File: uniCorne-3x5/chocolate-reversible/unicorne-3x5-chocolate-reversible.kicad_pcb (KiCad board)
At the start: 2 copper layers, 114.7 x 91.4 mm, 87 parts, among them J1 MJ-4PP-9, J2 Conn_01x05, J3 Conn_01x02, J4 Conn_01x03, SW1 SW_CHOC_HS, SW10 SW_CHOC_HS, SW11 SW_CHOC_HS, SW12 SW_CHOC_HS, SW13 SW_CHOC_HS, SW14 SW_CHOC_HS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

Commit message: amended chocolate 3x5
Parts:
- U1: footprint TB2086_MISC:ProMicro-ish-dn-rev-unrouted_3x5 -> TB2086_MISC:ProMicro-ish-dn-rev-unrouted_3x6
- moved R3 1.75 mm to (183.5, 110.0)
- moved R4 1.75 mm to (183.5, 111.9)
- moved JP9 1.22 mm to (187.7, 111.0)
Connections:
- PSW1 pad 1: unconnected-(PSW1-A-Pad1) -> BAT+
- PSW1 pad 3: BAT+ -> unconnected-(PSW1-C-Pad3)
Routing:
- net unconnected-(U1-RAW-Pad24): track 29.2 -> 11.0 mm
- net DATA: track 64.2 -> 75.9 mm
- net unconnected-(PSW1-C-Pad3): track 0.00 -> 6.49 mm
- net unconnected-(PSW1-A-Pad1): track 6.23 -> 0.00 mm
- net LED: track 61.5 -> 65.6 mm, vias 4 -> 5
- net BAT+: track 17.4 -> 14.1 mm
- net col2: track 192.9 -> 195.2 mm
- net unconnected-(U1-B3-Pad15): track 18.6 -> 16.5 mm
- net SDA: track 72.7 -> 70.8 mm
- net SCL: track 59.4 -> 61.2 mm
- net GND: track 45.4 -> 46.7 mm, vias 23 -> 24
- net Net-(JP9-C): track 16.3 -> 15.4 mm
- net col0: track 206.5 -> 205.6 mm
- net col1: track 187.2 -> 186.5 mm
- net row0: track 147.8 -> 148.2 mm, vias 1 -> 2
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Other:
- board text added: "uniCorne Choc 3x5"
- board text removed: "uniCorne Choc"

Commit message: small tweak
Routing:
- net RESET: track 59.3 -> 61.7 mm
- net IS_LEFT: track 24.6 -> 22.3 mm
- net unconnected-(PSW1-C-Pad3): track 6.49 -> 5.34 mm
- net Net-(JP9-C): track 15.4 -> 14.4 mm
- net SCL: track 61.2 -> 60.3 mm
- net SDA: track 70.8 -> 70.1 mm
- net col4: track 136.5 -> 135.9 mm
- net DATA: track 75.9 -> 75.3 mm
- net GND: track 46.7 -> 46.3 mm, vias 24 -> 23

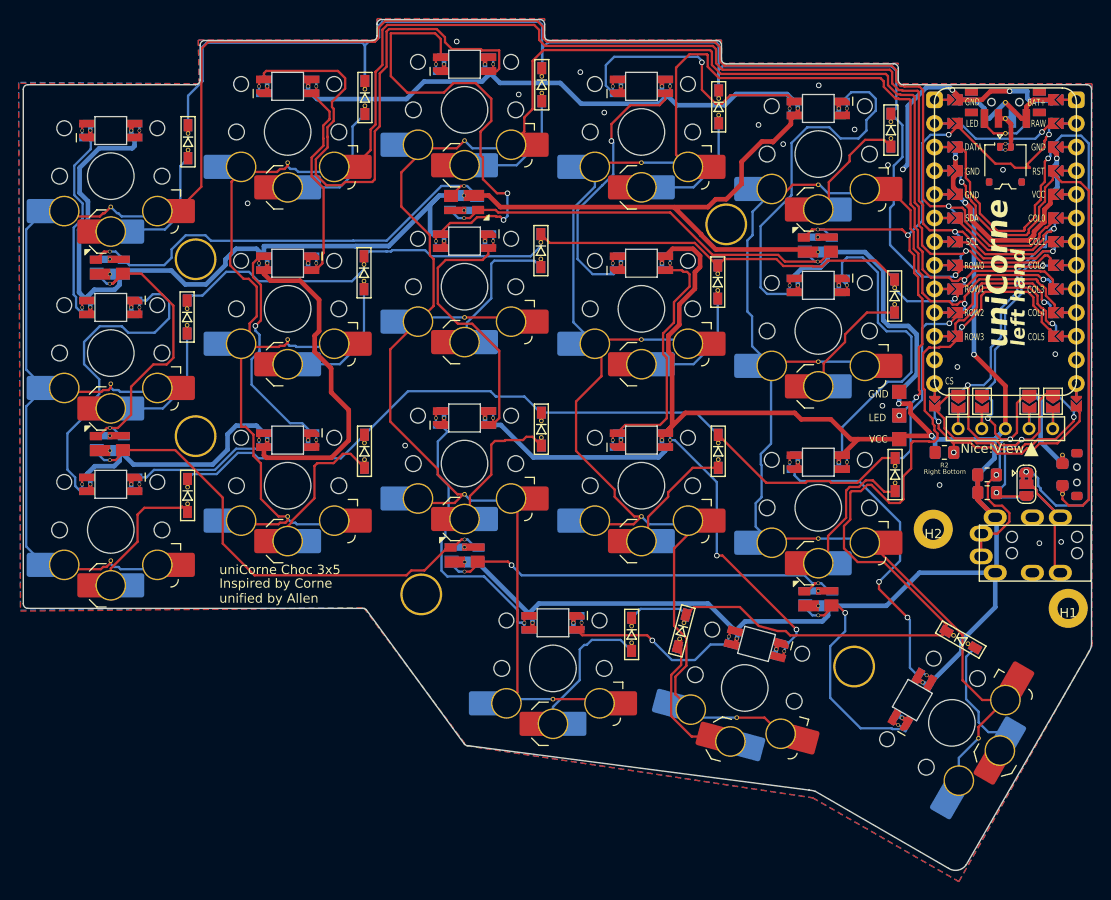
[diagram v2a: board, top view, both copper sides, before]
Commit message: amended footprint for LED
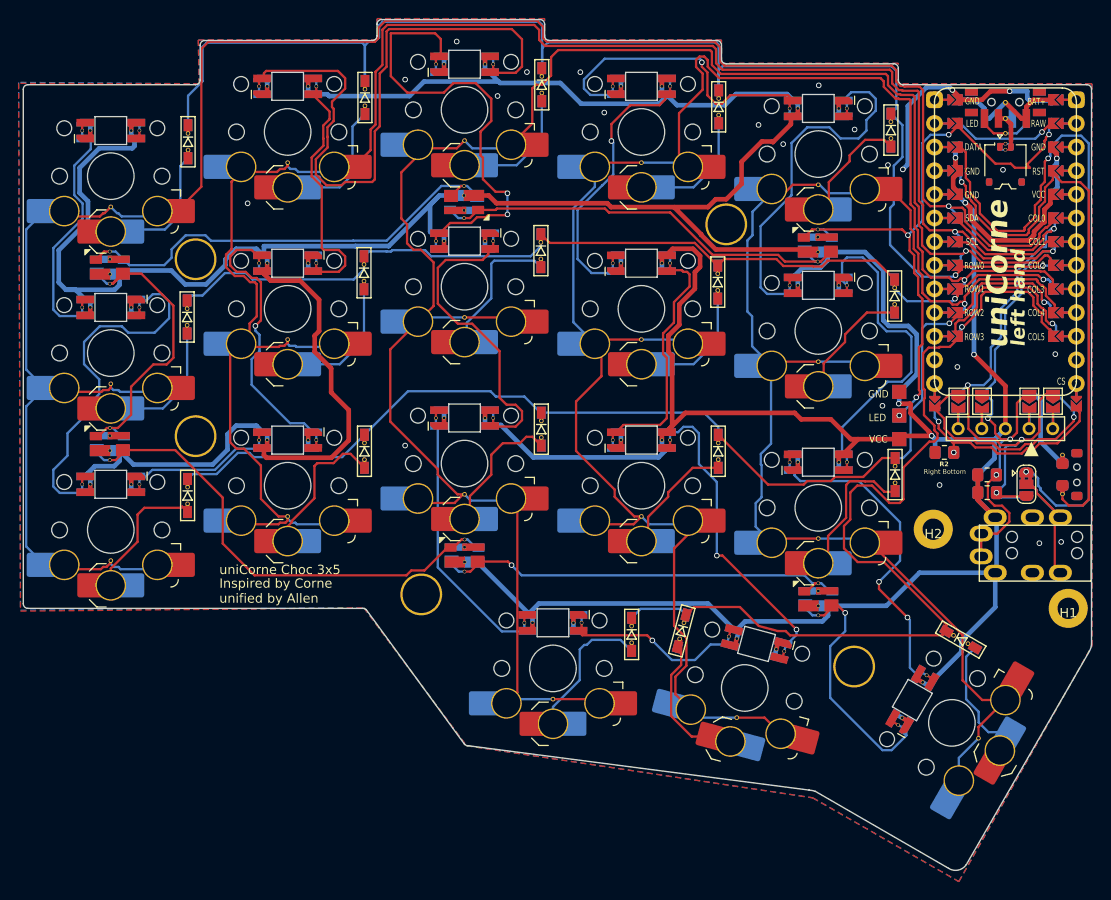
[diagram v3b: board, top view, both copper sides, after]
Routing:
- net Net-(L12-DIN): track 23.6 -> 29.0 mm
- net Net-(L2-DIN): track 61.9 -> 66.9 mm
- net Net-(L13-DOUT): track 27.5 -> 31.9 mm
- net Net-(L2-DOUT): track 21.5 -> 25.8 mm
- net Net-(L4-DIN): track 28.6 -> 32.3 mm
- net Net-(L1-DIN): track 21.1 -> 24.4 mm
- net Net-(L14-DOUT): track 28.5 -> 31.6 mm
- net Net-(L11-DOUT): track 35.6 -> 38.2 mm
- net Net-(L18-DIN): track 25.2 -> 27.7 mm
- net VCC: track 518.8 -> 521.2 mm
- net col1: track 186.0 -> 188.0 mm
- net Net-(L13-DIN): track 29.3 -> 27.5 mm
- net col3: track 178.0 -> 176.7 mm
- net row3: track 109.4 -> 108.3 mm
- net CS: track 25.9 -> 25.0 mm
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
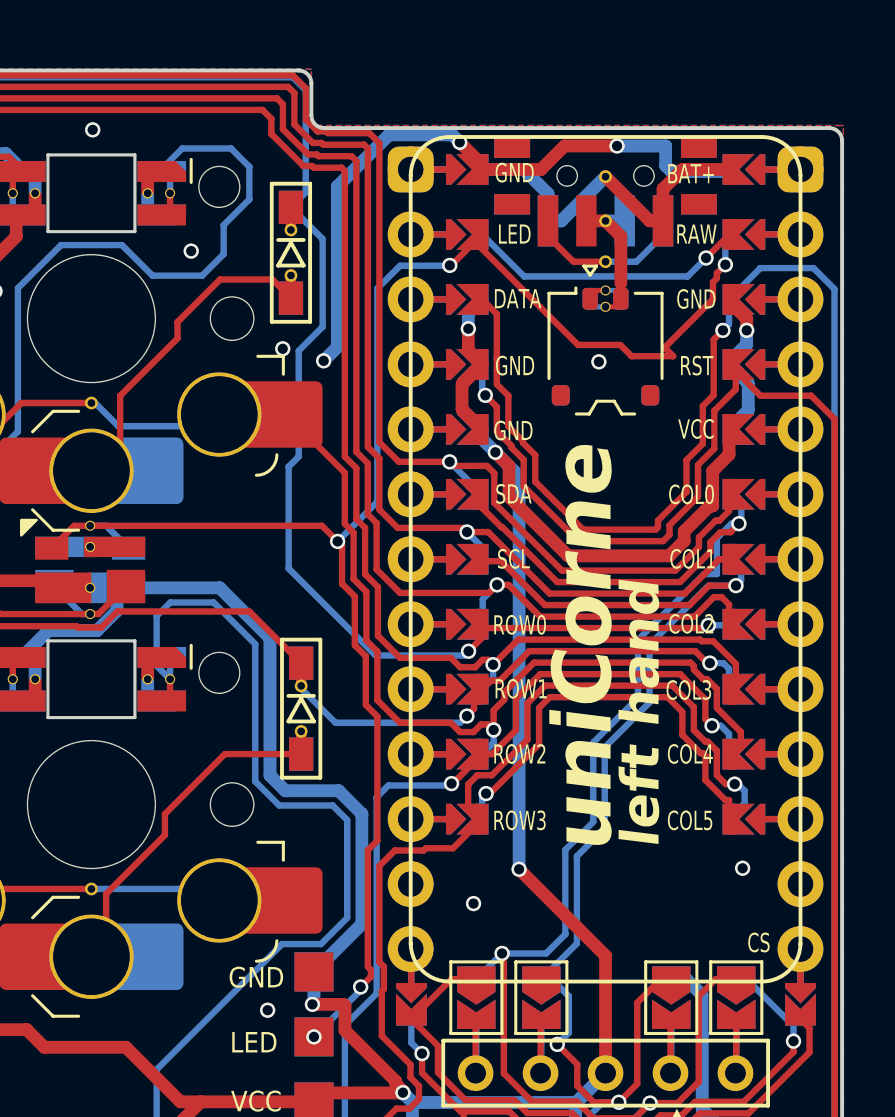
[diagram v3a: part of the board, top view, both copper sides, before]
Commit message: fixed footprint for promicro-ish 3x6
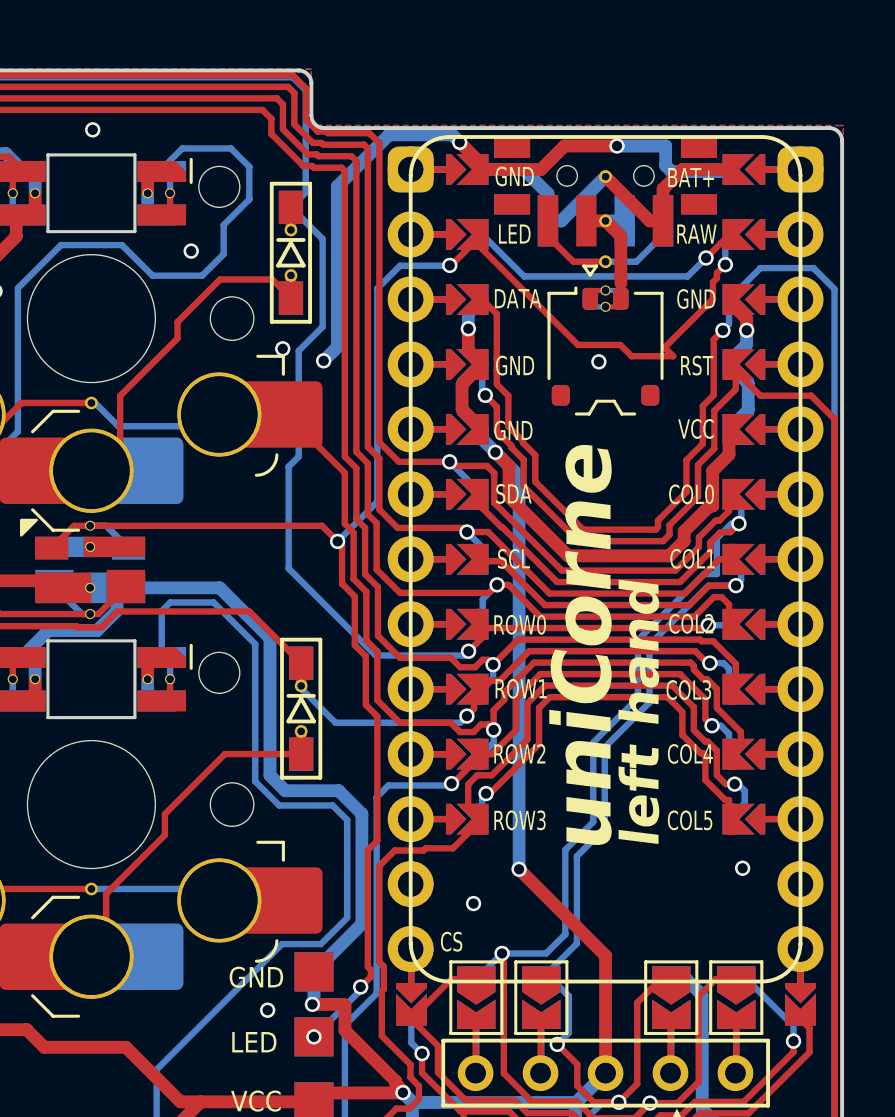
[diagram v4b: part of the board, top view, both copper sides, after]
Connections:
- U1 pad 12: IS_LEFT -> CS
- U1 pad 13: CS -> IS_LEFT
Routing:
- net Net-(L10-DIN): track 33.7 -> 32.6 mm

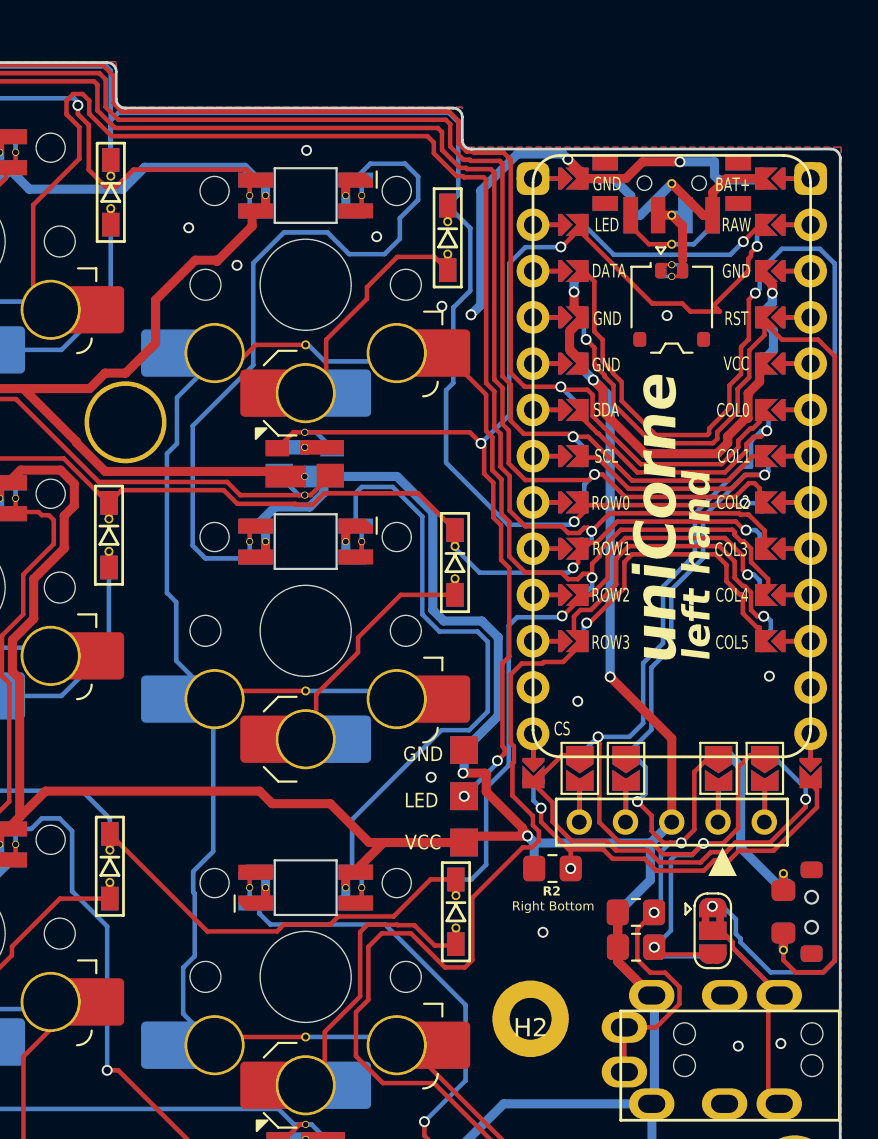
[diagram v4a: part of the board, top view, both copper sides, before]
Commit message: Bug fix scl (#3)
* fixed 3x5 hyprid mx

* fixed 3x5

* fixed 3x6
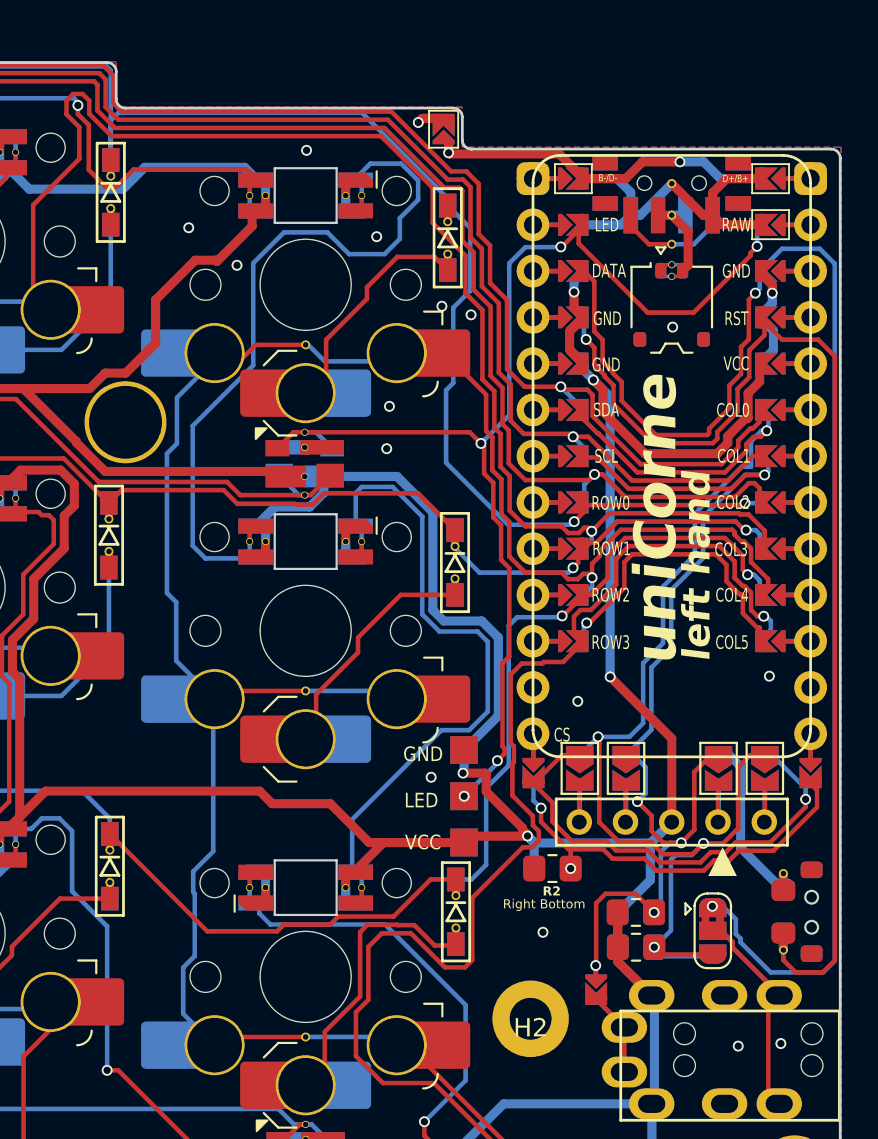
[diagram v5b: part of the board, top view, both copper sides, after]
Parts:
- added JP10: , TB2086_MISC:SolderJumper-2_P1.3mm_Open_TrianglePad1.0x1.2mm_rev, F.Cu at (181.3, 114.2)
- added JP11: , TB2086_MISC:SolderJumper-2_P1.3mm_Open_TrianglePad1.0x1.2mm_rev, F.Cu at (172.9, 67.0)
- U1: footprint TB2086_MISC:ProMicro-ish-dn-rev-unrouted_3x6 -> TB2086_MISC:ProMicro-ish-dn-rev-unrouted_3x5
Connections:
- J1 pad A: SCL -> Net-(JP10-B)
- U1 pad 24: unconnected-(U1-RAW-Pad24) -> BAT+
- U1 pad 26: GND -> B-/D-
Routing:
- net GND: track 46.3 -> 24.3 mm, vias 25 -> 26
- net B-/D-: track 0.00 -> 20.4 mm, vias 0 -> 2
- net unconnected-(U1-RAW-Pad24): track 11.0 -> 0.00 mm, vias 1 -> 0
- net Net-(JP10-B): track 0.00 -> 6.78 mm
- net BAT+: track 14.1 -> 19.8 mm
- net SCL: track 60.3 -> 56.5 mm, vias 4 -> 5
- net row0: track 148.1 -> 144.8 mm
- net col0: track 205.6 -> 203.1 mm
- net col1: track 188.0 -> 185.5 mm
- net col3: track 176.7 -> 174.4 mm
- net col2: track 195.2 -> 193.0 mm
- net Net-(J3-Pin_2): track 4.19 -> 5.04 mm
- net LED: track 65.6 -> 65.0 mm
